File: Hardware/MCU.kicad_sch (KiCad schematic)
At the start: 11 parts, among them J1 485, J4 Conn_01x06_MountingPin, U2 MAX3485, U6 CW32F030K8

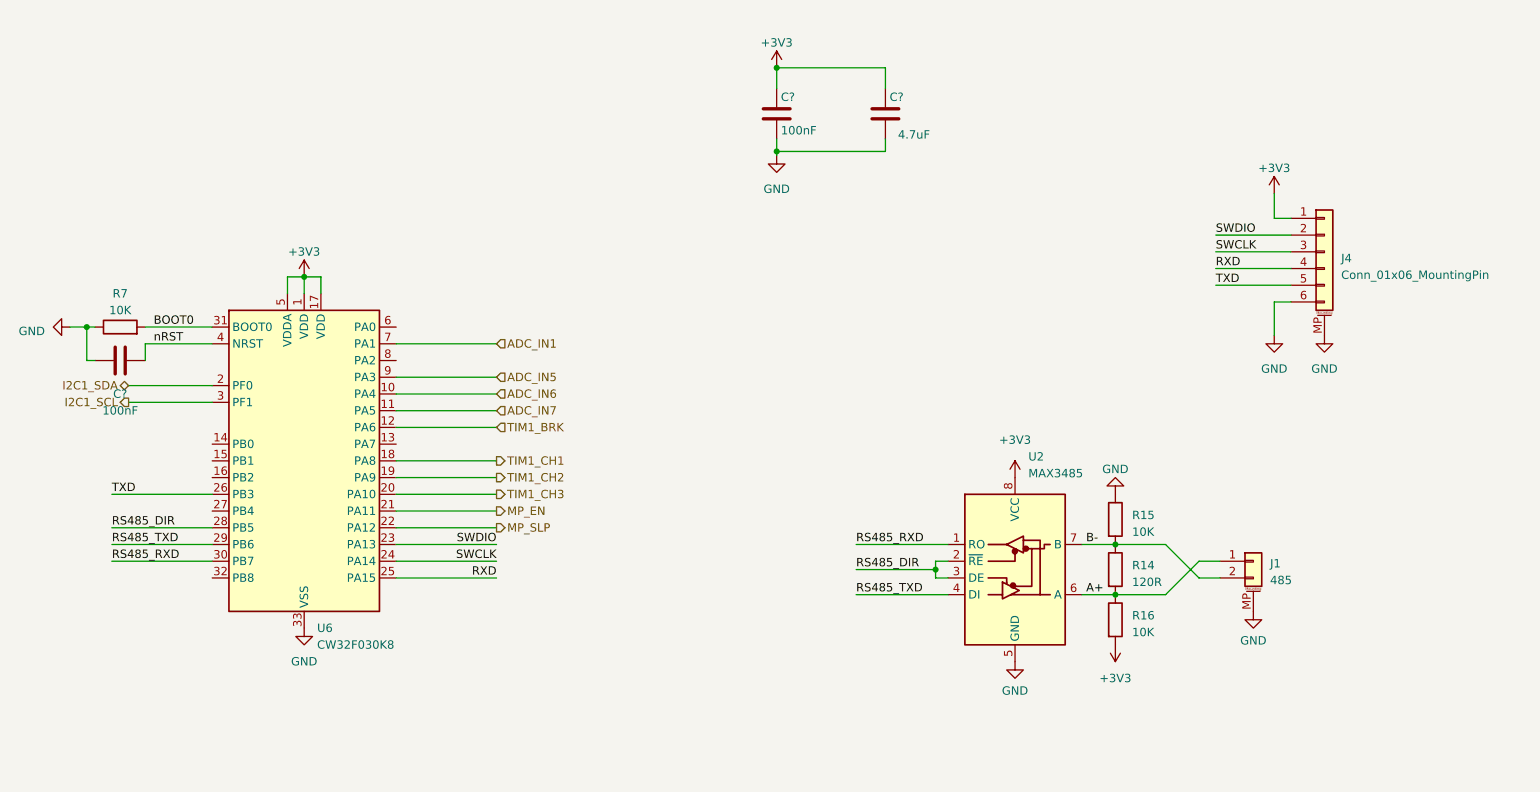
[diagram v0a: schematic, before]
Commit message: 完成原理图设计，完成初步布局布线
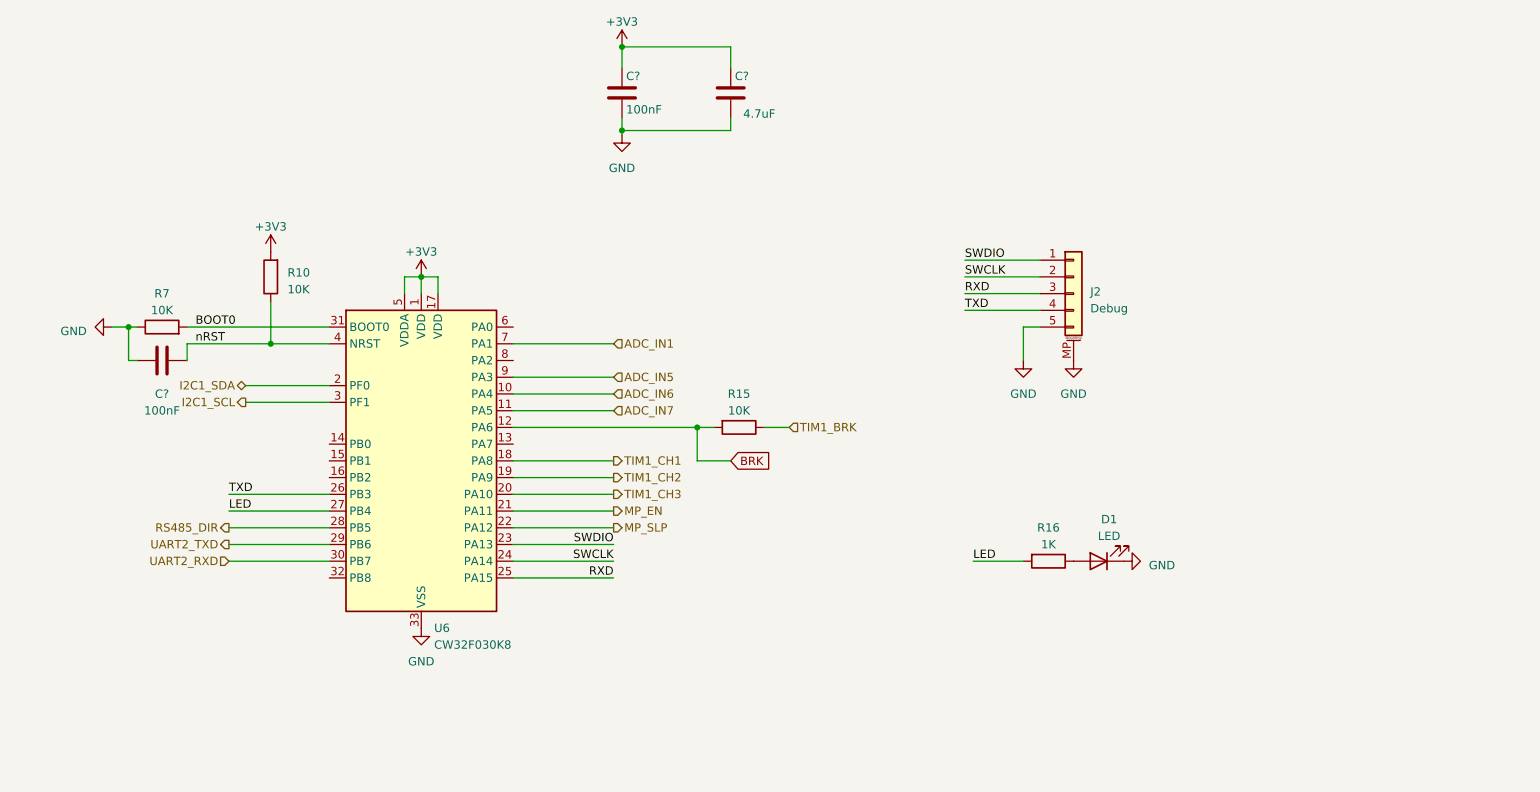
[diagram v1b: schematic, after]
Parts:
- removed J1: 485, Connector_JST:JST_GH_SM02B-GHS-TB_1x02-1MP_P1.25mm_Horizontal, symbol Connector_Generic_MountingPin:Conn_01x02_MountingPin
- removed J4: Conn_01x06_MountingPin, Connector_JST:JST_GH_SM06B-GHS-TB_1x06-1MP_P1.25mm_Horizontal, symbol Connector_Generic_MountingPin:Conn_01x06_MountingPin
- removed R14: 120R, myDevice:0603_R, symbol Device:R
- removed U2: MAX3485, Package_SO:SOIC-8_3.9x4.9mm_P1.27mm, symbol Interface_UART:MAX3485
- added D1: LED, myDevice:0603_LED, symbol Device:LED
- added J2: Debug, Connector_JST:JST_SH_BM05B-SRSS-TB_1x05-1MP_P1.00mm_Vertical, symbol Connector_Generic_MountingPin:Conn_01x05_MountingPin
- added R10: 10K, myDevice:0603_R, symbol Device:R
- R16: value 10K -> 1K
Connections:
- net +3V3: now also R10.2; no longer R16.2
- net GND: now also D1.1 (K), J2.5 (Pin_5), J2.MP (MountPin); no longer R15.1
- net RXD: now also J2.3 (Pin_3)
- net SWCLK: now also J2.2 (Pin_2)
- net SWDIO: now also J2.1 (Pin_1)
- net TIM1_BRK: now also R15.1; no longer U6.12 (PA6)
- net TXD: now also J2.4 (Pin_4)
- net nRST: now also R10.1
- net LED: now reaches U6.27 (PB4)
- net LED: now also R16.2
- net A+: no longer names the net of R16.1
- net A+: now also D1.2 (A)
- net B- renamed BRK
- net BRK: now also U6.12 (PA6)
- net RS485_RXD renamed UART2_RXD
- net RS485_TXD renamed UART2_TXD
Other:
- moved on the sheet: C?, R7, U6

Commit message: 完善原理图设计、添加硬件README
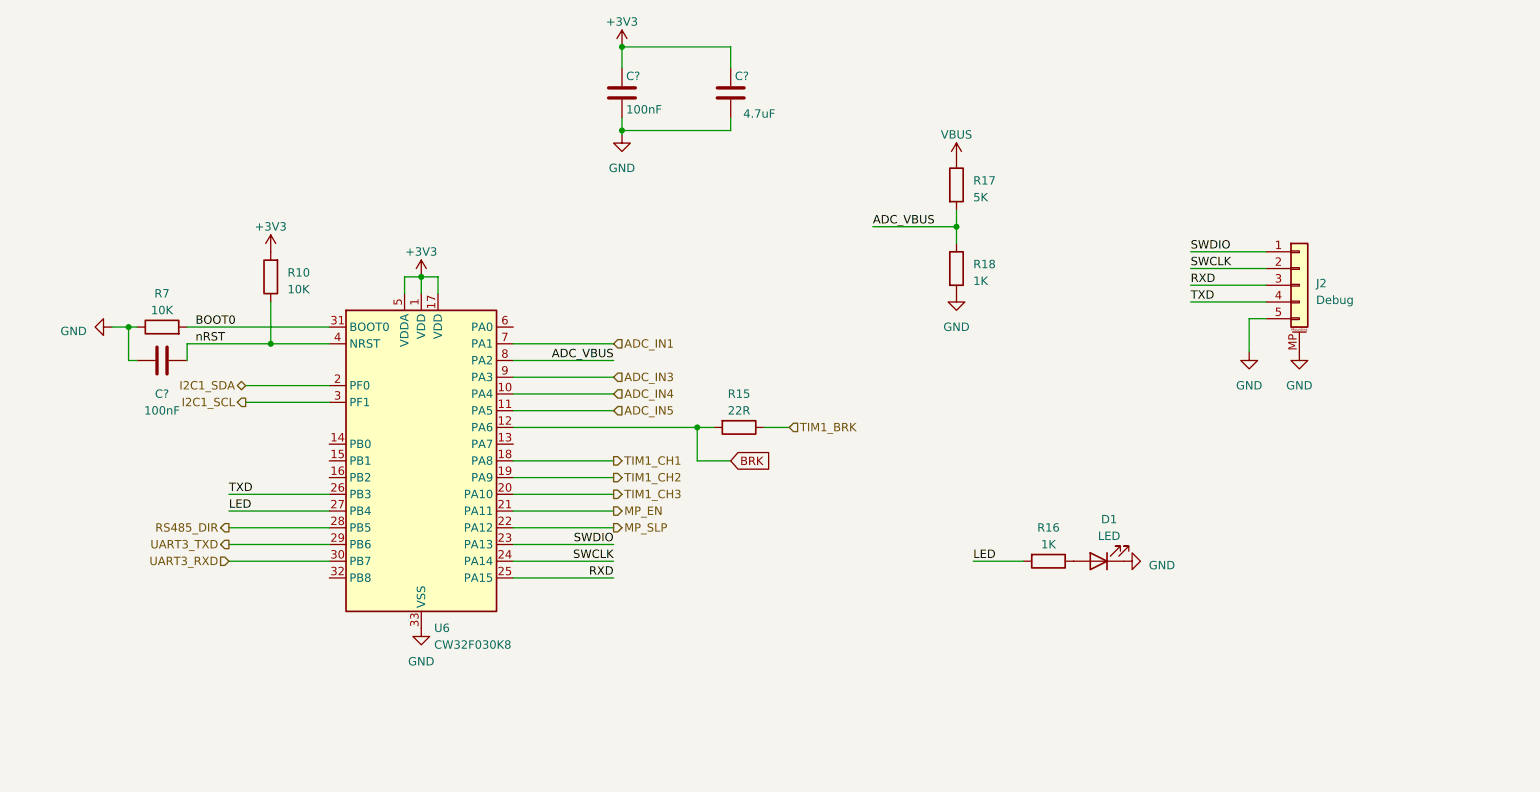
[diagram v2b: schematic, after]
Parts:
- added R17: 5K, myDevice:0603_R, symbol Device:R
- added R18: 1K, myDevice:0603_R, symbol Device:R
- R15: value 10K -> 22R
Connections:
- net ADC_IN7 is gone; now on net ADC_IN5: U6.11 (PA5)
- net ADC_IN5: no longer U6.9 (PA3)
- net GND: now also R18.2
- net ADC_VBUS: now reaches U6.8 (PA2)
- net ADC_VBUS: now also R17.2, R18.1
- net ADC_IN6 renamed ADC_IN4
- net UART2_RXD renamed UART3_RXD
- net UART2_TXD renamed UART3_TXD
- new net ADC_IN3: U6.9 (PA3)
- new net VBUS: R17.1
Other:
- moved on the sheet: J2

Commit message: 基本完成PCB设计
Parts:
- added C?: 100nF, myDevice:0603_C, symbol Device:C
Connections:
- net +3V3: now also C?.1
- net GND: now also J2.1 (Pin_1), C?.2; no longer J2.5 (Pin_5)
- net SWCLK: now also J2.4 (Pin_4); no longer J2.2 (Pin_2)
- net SWDIO: now also J2.5 (Pin_5); no longer J2.1 (Pin_1)
- net TXD: now also J2.2 (Pin_2); no longer J2.4 (Pin_4)
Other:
- moved on the sheet: C?, J2

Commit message: 第一版硬件做好啦！(●'◡'●)
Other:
- company: (none) -> Akako Industry
- title: (none) -> cwFOC/MCU
- moved on the sheet: C?, D1, J2, R10, R15, R16, R17, R18, R7, U6

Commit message: 调整第二版原理图
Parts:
- removed J2: Debug, Connector_JST:JST_SH_BM05B-SRSS-TB_1x05-1MP_P1.00mm_Vertical, symbol Connector_Generic_MountingPin:Conn_01x05_MountingPin
- added J2: Conn_01x06_MountingPin, Connector_JST:JST_GH_SM06B-GHS-TB_1x06-1MP_P1.25mm_Horizontal, symbol Connector_Generic_MountingPin:Conn_01x06_MountingPin
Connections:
- net GND: now also J2.6 (Pin_6), J2.MP (MountPin)
- net RXD: now also J2.3 (Pin_3)
- net SWCLK: now also J2.2 (Pin_2)
- net SWDIO: now also J2.1 (Pin_1)
- net TXD: now also J2.4 (Pin_4)
- net nRST: now also J2.5 (Pin_5)
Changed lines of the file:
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@@
+    (stroke (width 0) (type default))
+  )
+  (wire (pts (xy 200.66 110.49) (xy 212.09 110.49))
     (stroke (width 0) (type default))
   )
@@
     (stroke (width 0) (type default))
   )
-  (wire (pts (xy 212.09 110.49) (xy 209.55 110.49))
+  (wire (pts (xy 212.09 113.03) (xy 209.55 113.03))
     (stroke (width 0) (type default))
   )
@@
     (stroke (width 0) (type default))
   )
-  (wire (pts (xy 209.55 110.49) (xy 209.55 115.57))
+  (wire (pts (xy 209.55 113.03) (xy 209.55 118.11))
     (stroke (width 0) (type default))
   )
@@
   )
   (label "BOOT0" (at 81.28 99.06 0) (fields_autoplaced)
+    (effects (font (size 1.27 1.27)) (justify left bottom))
+  )
+  (label "nRST" (at 200.66 110.49 0) (fields_autoplaced)
     (effects (font (size 1.27 1.27)) (justify left bottom))
   )
@@
     )
   )
+  (symbol (lib_id "Connector_Generic_MountingPin:Conn_01x06_MountingPin") (at 217.17 105.41 0) (unit 1)
+    (in_bom yes) (on_board yes) (dnp no) (fields_autoplaced)
+    (property "Reference" "J2" (at 219.71 106.4006 0)
+      (effects (font (size 1.27 1.27)) (justify left))
+    )
+    (property "Value" "Conn_01x06_MountingPin" (at 219.71 108.9406 0)
+      (effects (font (size 1.27 1.27)) (justify left))
+    )
+    (property "Footprint" "Connector_JST:JST_GH_SM06B-GHS-TB_1x06-1MP_P1.25mm_Horizontal" (at 217.17 105.41 0)
+      (effects (font (size 1.27 1.27)) hide)
+    )
+    (property "Datasheet" "~" (at 217.17 105.41 0)
+      (effects (font (size 1.27 1.27)) hide)
+    )
+    (pin "1")
+    (pin "2")
+    (pin "3")
+    (pin "4")
+    (pin "5")
+    (pin "6")
+    (pin "MP")
+    (instances
+      (project "cwFOC"
+        (path "/ff847474-9801-42c6-af12-b4b1b75aa0af/1a00d99a-20c9-415d-b828-323b0b58b185"
+          (reference "J2") (unit 1)
+        )
+      )
+    )
+  )
   (symbol (lib_id "power:VBUS") (at 190.5 55.88 0) (unit 1)
     (in_bom yes) (on_board yes) (dnp no) (fields_autoplaced)
@@
     )
   )
-  (symbol (lib_id "power:GND") (at 217.17 95.25 180) (unit 1)
-    (in_bom yes) (on_board yes) (dnp no) (fields_autoplaced)
-    (property "Reference" "#PWR041" (at 217.17 88.9 0)
-      (effects (font (size 1.27 1.27)) hide)
-    )
-    (property "Value" "GND" (at 217.17 91.44 0)
-      (effects (font (size 1.27 1.27)))
-    )
-    (property "Footprint" "" (at 217.17 95.25 0)
-      (effects (font (size 1.27 1.27)) hide)
-    )
-    (property "Datasheet" "" (at 217.17 95.25 0)
+  (symbol (lib_id "power:GND") (at 217.17 118.11 0) (unit 1)
+    (in_bom yes) (on_board yes) (dnp no) (fields_autoplaced)
+    (property "Reference" "#PWR041" (at 217.17 124.46 0)
+      (effects (font (size 1.27 1.27)) hide)
+    )
+    (property "Value" "GND" (at 219.71 120.015 0)
+      (effects (font (size 1.27 1.27)) (justify left))
+    )
+    (property "Footprint" "" (at 217.17 118.11 0)
+      (effects (font (size 1.27 1.27)) hide)
+    )
+    (property "Datasheet" "" (at 217.17 118.11 0)
       (effects (font (size 1.27 1.27)) hide)
     )
@@
     )
   )
-  (symbol (lib_id "power:GND") (at 209.55 115.57 0) (unit 1)
-    (in_bom yes) (on_board yes) (dnp no) (fields_autoplaced)
-    (property "Reference" "#PWR042" (at 209.55 121.92 0)
-      (effects (font (size 1.27 1.27)) hide)
-    )
-    (property "Value" "GND" (at 209.55 120.65 0)
-      (effects (font (size 1.27 1.27)))
-    )
-    (property "Footprint" "" (at 209.55 115.57 0)
-      (effects (font (size 1.27 1.27)) hide)
-    )
-    (property "Datasheet" "" (at 209.55 115.57 0)
+  (symbol (lib_id "power:GND") (at 209.55 118.11 0) (unit 1)
+    (in_bom yes) (on_board yes) (dnp no) (fields_autoplaced)
+    (property "Reference" "#PWR042" (at 209.55 124.46 0)
+      (effects (font (size 1.27 1.27)) hide)
+    )
+    (property "Value" "GND" (at 209.55 123.19 0)
+      (effects (font (size 1.27 1.27)))
+    )
+    (property "Footprint" "" (at 209.55 118.11 0)
+      (effects (font (size 1.27 1.27)) hide)
+    )
+    (property "Datasheet" "" (at 209.55 118.11 0)
       (effects (font (size 1.27 1.27)) hide)
     )
@@
         )
       )
-    )
-  )
-  (symbol (lib_id "Connector_Generic_MountingPin:Conn_01x05_MountingPin") (at 217.17 105.41 0) (mirror x) (unit 1)
-    (in_bom yes) (on_board yes) (dnp no)
-    (property "Reference" "J2" (at 219.71 105.6894 0)
-      (effects (font (size 1.27 1.27)) (justify left))
-    )
-    (property "Value" "Debug" (at 219.71 103.1494 0)
-      (effects (font (size 1.27 1.27)) (justify left))
-    )
-    (property "Footprint" "Connector_JST:JST_SH_BM05B-SRSS-TB_1x05-1MP_P1.00mm_Vertical" (at 217.17 105.41 0)
-      (effects (font (size 1.27 1.27)) hide)
-    )
-    (property "Datasheet" "~" (at 217.17 105.41 0)
-      (effects (font (size 1.27 1.27)) hide)
-    )
-    (pin "1")
-    (pin "2")
-    (pin "3")
-    (pin "4")
-    (pin "5")
-    (pin "MP")
-    (instances
-      (project "cwFOC"
-        (path "/ff847474-9801-42c6-af12-b4b1b75aa0af/1a00d99a-20c9-415d-b828-323b0b58b185"
-          (reference "J2") (unit 1)
-        )
-      )

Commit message: 小修小补，拉了点线
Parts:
- R15: value 22R -> 470R
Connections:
- net ADC_IN1: no longer names the net of U6.7 (PA1)
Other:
- company: Akako Industry -> Akako Science & Industry
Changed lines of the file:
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@@
     (date "2023-03-19")
     (rev "1.0")
-    (company "Akako Industry")
+    (company "Akako Science & Industry")
     (comment 1 "赤紫绮")
     (comment 2 "赤紫绮")
@@
   )
   (hierarchical_label "TIM1_BRK" (shape input) (at 171.45 114.3 0) (fields_autoplaced)
-    (effects (font (size 1.27 1.27)) (justify left))
-  )
-  (hierarchical_label "ADC_IN1" (shape input) (at 144.78 101.6 0) (fields_autoplaced)
     (effects (font (size 1.27 1.27)) (justify left))
   )
@@
       (effects (font (size 1.27 1.27)))
     )
-    (property "Value" "22R" (at 163.83 111.76 90)
+    (property "Value" "470R" (at 163.83 111.76 90)
       (effects (font (size 1.27 1.27)))
     )

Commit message: 完成第二版硬件
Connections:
- net GND: now also J2.1 (Pin_1); no longer J2.6 (Pin_6)
- net RXD: now also J2.4 (Pin_4); no longer J2.3 (Pin_3)
- net SWCLK: now also J2.5 (Pin_5); no longer J2.2 (Pin_2)
- net SWDIO: now also J2.6 (Pin_6); no longer J2.1 (Pin_1)
- net TXD: now also J2.3 (Pin_3); no longer J2.4 (Pin_4)
- net nRST: now also J2.2 (Pin_2); no longer J2.5 (Pin_5)
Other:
- moved on the sheet: J2
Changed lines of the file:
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@@
     )
   )
-  (symbol (lib_id "Connector_Generic_MountingPin:Conn_01x06_MountingPin") (at 217.17 105.41 0) (unit 1)
-    (in_bom yes) (on_board yes) (dnp no) (fields_autoplaced)
-    (property "Reference" "J2" (at 219.71 106.4006 0)
+  (symbol (lib_id "Connector_Generic_MountingPin:Conn_01x06_MountingPin") (at 217.17 107.95 0) (mirror x) (unit 1)
+    (in_bom yes) (on_board yes) (dnp no)
+    (property "Reference" "J2" (at 219.71 106.9594 0)
       (effects (font (size 1.27 1.27)) (justify left))
     )
-    (property "Value" "Conn_01x06_MountingPin" (at 219.71 108.9406 0)
+    (property "Value" "Conn_01x06_MountingPin" (at 219.71 104.4194 0)
       (effects (font (size 1.27 1.27)) (justify left))
     )
-    (property "Footprint" "Connector_JST:JST_GH_SM06B-GHS-TB_1x06-1MP_P1.25mm_Horizontal" (at 217.17 105.41 0)
+    (property "Footprint" "Connector_JST:JST_GH_SM06B-GHS-TB_1x06-1MP_P1.25mm_Horizontal" (at 217.17 107.95 0)
       (effects (font (size 1.27 1.27)) hide)
     )
-    (property "Datasheet" "~" (at 217.17 105.41 0)
+    (property "Datasheet" "~" (at 217.17 107.95 0)
       (effects (font (size 1.27 1.27)) hide)
     )
@@
     )
   )
-  (symbol (lib_id "power:GND") (at 217.17 118.11 0) (unit 1)
+  (symbol (lib_id "power:GND") (at 217.17 95.25 180) (unit 1)
     (in_bom yes) (on_board yes) (dnp no) (fields_autoplaced)
-    (property "Reference" "#PWR041" (at 217.17 124.46 0)
+    (property "Reference" "#PWR041" (at 217.17 88.9 0)
       (effects (font (size 1.27 1.27)) hide)
     )
-    (property "Value" "GND" (at 219.71 120.015 0)
-      (effects (font (size 1.27 1.27)) (justify left))
+    (property "Value" "GND" (at 217.17 91.44 0)
+      (effects (font (size 1.27 1.27)))
     )
-    (property "Footprint" "" (at 217.17 118.11 0)
+    (property "Footprint" "" (at 217.17 95.25 0)
       (effects (font (size 1.27 1.27)) hide)
     )
-    (property "Datasheet" "" (at 217.17 118.11 0)
+    (property "Datasheet" "" (at 217.17 95.25 0)
       (effects (font (size 1.27 1.27)) hide)
     )
